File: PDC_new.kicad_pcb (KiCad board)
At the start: 2 copper layers, 97 parts, among them J1 Conn_01x02_Pin, J10 Conn_01x02_Pin, J12 Conn_01x02_Pin, J13 XT90PW-F, J14 B2B-XH-A__LF__SN_, J15 Conn_01x02, J2 Conn_01x02_Pin, J3 Conn_01x02_Pin, J4 Conn_01x02_Pin, J5 Conn_01x02_Pin, J6 Conn_01x02_Pin, J7 Conn_01x02_Pin, J8 Conn_01x02_Pin, J9 Conn_01x02_Pin, Q1 BSS123, Q2 IRF540NSTRLPBF, U1 TPSI3050QDWZRQ1, U10 LM393LVDR, U11 IPB017N10N5ATMA1, U12 IPB017N10N5ATMA1, U13 XT90PW(2+2)-M.G.Y, U14 IPB017N10N5ATMA1, U2 TPSI3050QDWZRQ1, U3 TPSI3050QDWZRQ1, U4 74HC74, U5 URB4805LD-60WR3, U6 IPB017N10N5ATMA1, U7 TLC555CDR, U8 SN74HC08D, U9 SN74HC14DR

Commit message: pcb: continue routing, add board outline, remove stray J15
Remove J15 footprint, which has no matching symbol in the schematic.
Mirror the same board into the top-level PDC_new.kicad_pcb.

Co-Authored-By: Claude Opus 5.5 <noreply@anthropic.com>
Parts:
- removed J15: Conn_01x02, Connector_JST:JST_XH_B2B-XH-A_1x02_P2.50mm_Vertical
- moved C6 196.5 mm to (341.1, 308.0)
- moved F1 189.6 mm to (243.0, 280.8)
- moved F3 184.7 mm to (281.5, 251.3)
- moved R4 178.8 mm to (308.9, 254.5)
- moved R6 176.4 mm to (304.0, 260.5)
- moved C18 170.2 mm to (345.0, 248.0)
- moved D5 162.2 mm to (314.0, 243.5), turned to 90 degrees
- moved C22 161.2 mm to (347.0, 231.5)
- moved R24 159.1 mm to (319.0, 236.4), turned to 90 degrees
- moved R22 158.0 mm to (308.9, 260.5)
- moved C25 154.9 mm to (330.0, 248.0)
- moved C19 146.8 mm to (319.0, 243.0), turned to 90 degrees
- moved R21 146.7 mm to (303.9, 255.0)
- moved C26 142.0 mm to (331.5, 232.0)
- moved C23 139.4 mm to (334.5, 216.0)
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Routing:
- net Net-(U3-VDDH): track 0.00 -> 3.13 mm

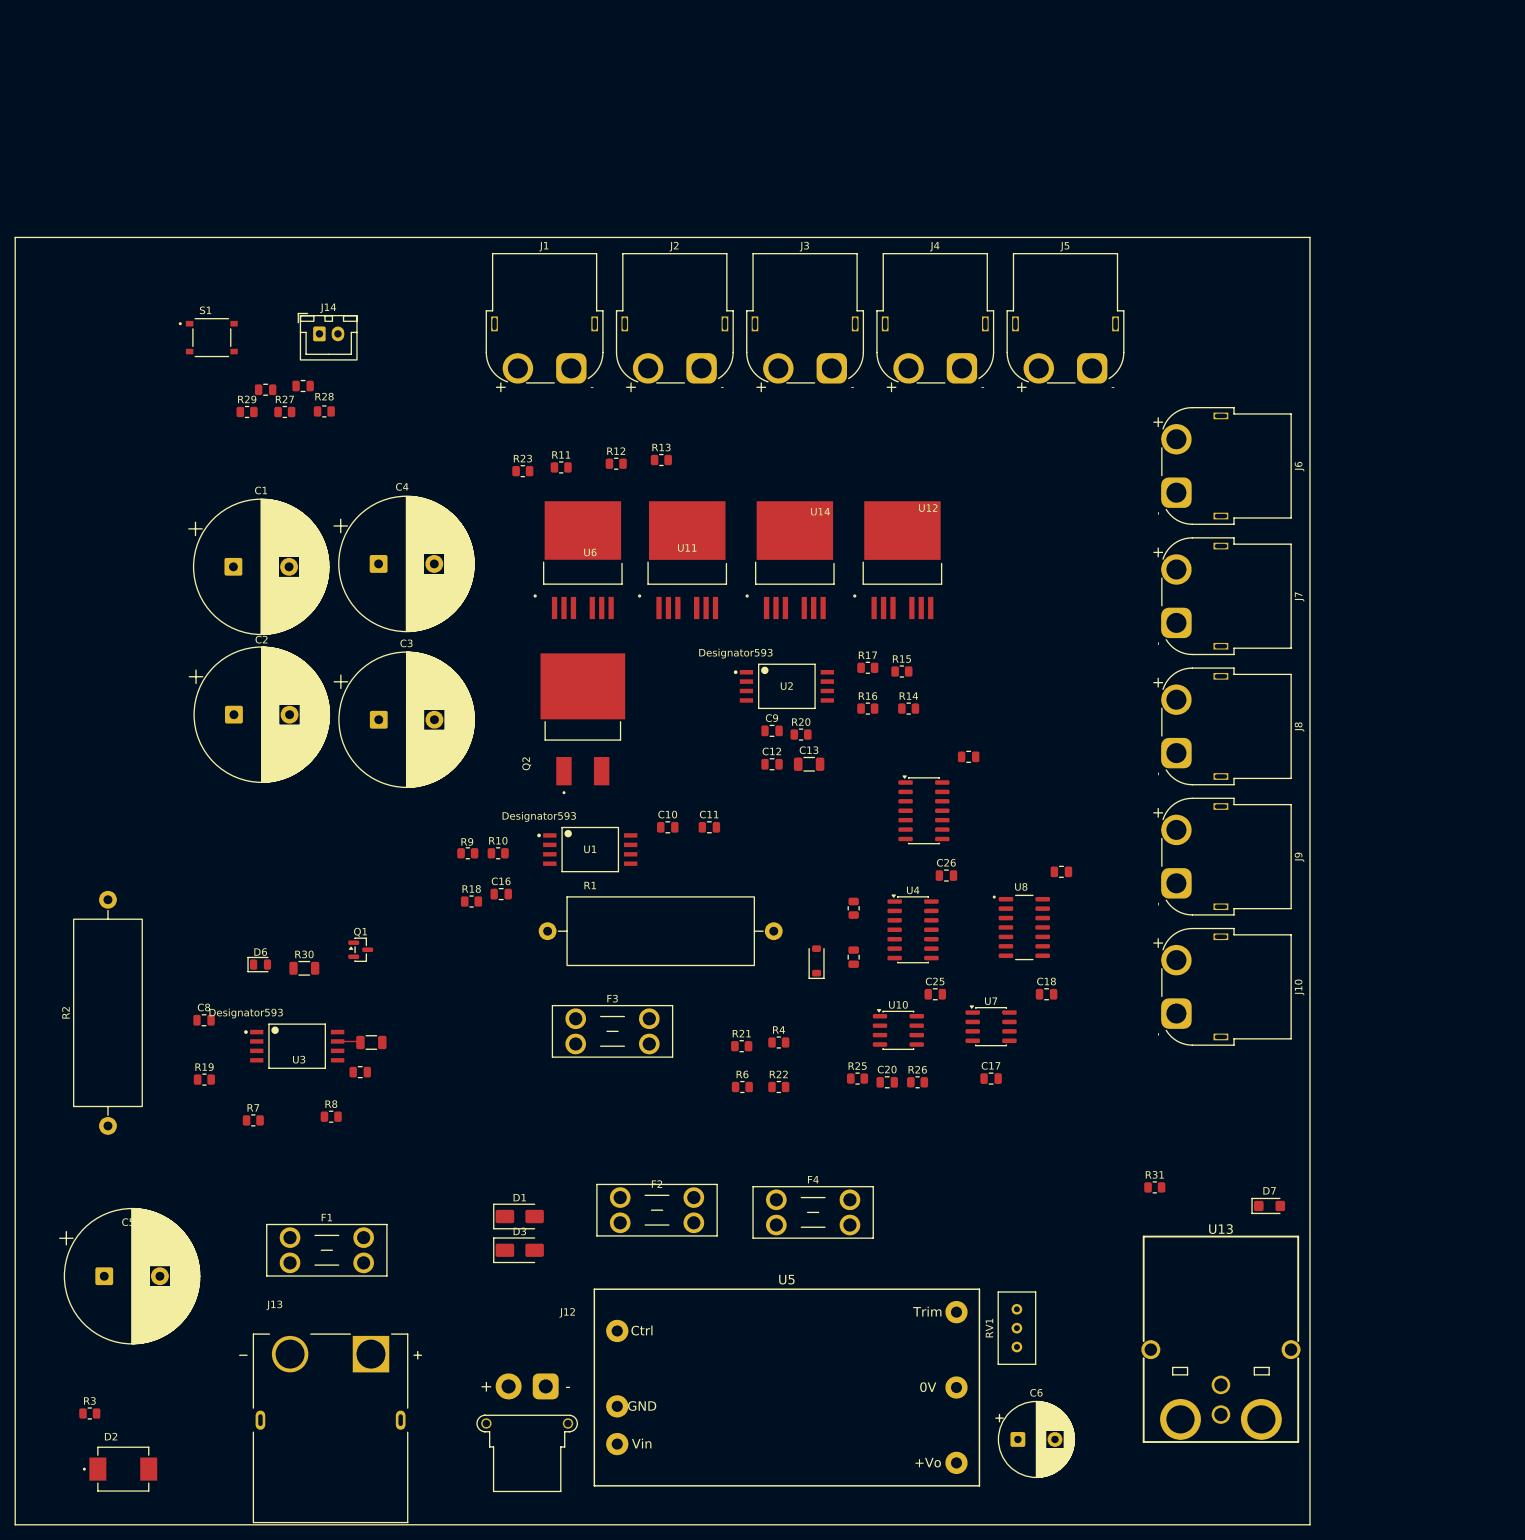
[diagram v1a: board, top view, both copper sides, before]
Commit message: Reorganize repo: move libraries into Libraries/, promote PDC_new (2) to main project
Libraries:
- Move all symbol/footprint folders into Libraries/: B2B-XH-A__LF__SN_,
  IRF540NSTRLPBF, SMCJ54A, SMCJ54CA-13-F, SN74HC08D, SN74HC14DR,
  TS-1187A-B-A-B, XT90PW-F, ul_LM393LVDR and pdc_new.pretty.
- Merge root ul_IPB017N10N5ATMA1/ and ul_TPSI3050QDWZRQ1/ into the existing
  folders in Libraries/ (KiCADv6 symbols/footprints moved in; duplicate
  readme.txt and ImportGuides.html at the root dropped).
- Update fp-lib-table and sym-lib-table to point at ${KIPRJMOD}/Libraries/.

Project files:
- Replace PDC_new.kicad_sch/.kicad_pcb/.kicad_pro with the latest
  PDC_new (2) versions and remove the PDC_new (2)/ folder.
- Move PDC_new (2)/report.txt to the repo root.
- Remove the stray extensionless "PDC_new" file (old schematic copy).
- Rename internal "PDC_new (2)" references (schematic instance project
  names, PCB sheetfile refs, project metadata) to "PDC_new".
- Change absolute C:/Users/... 3D model paths in the PCB to
  ${KIPRJMOD}/Libraries/... so they resolve on any machine.

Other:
- .history/ is already ignored by .gitignore (applies at any depth).
- Update README to describe the Libraries/ folder.

Co-Authored-By: Claude Opus 5.5 <noreply@anthropic.com>
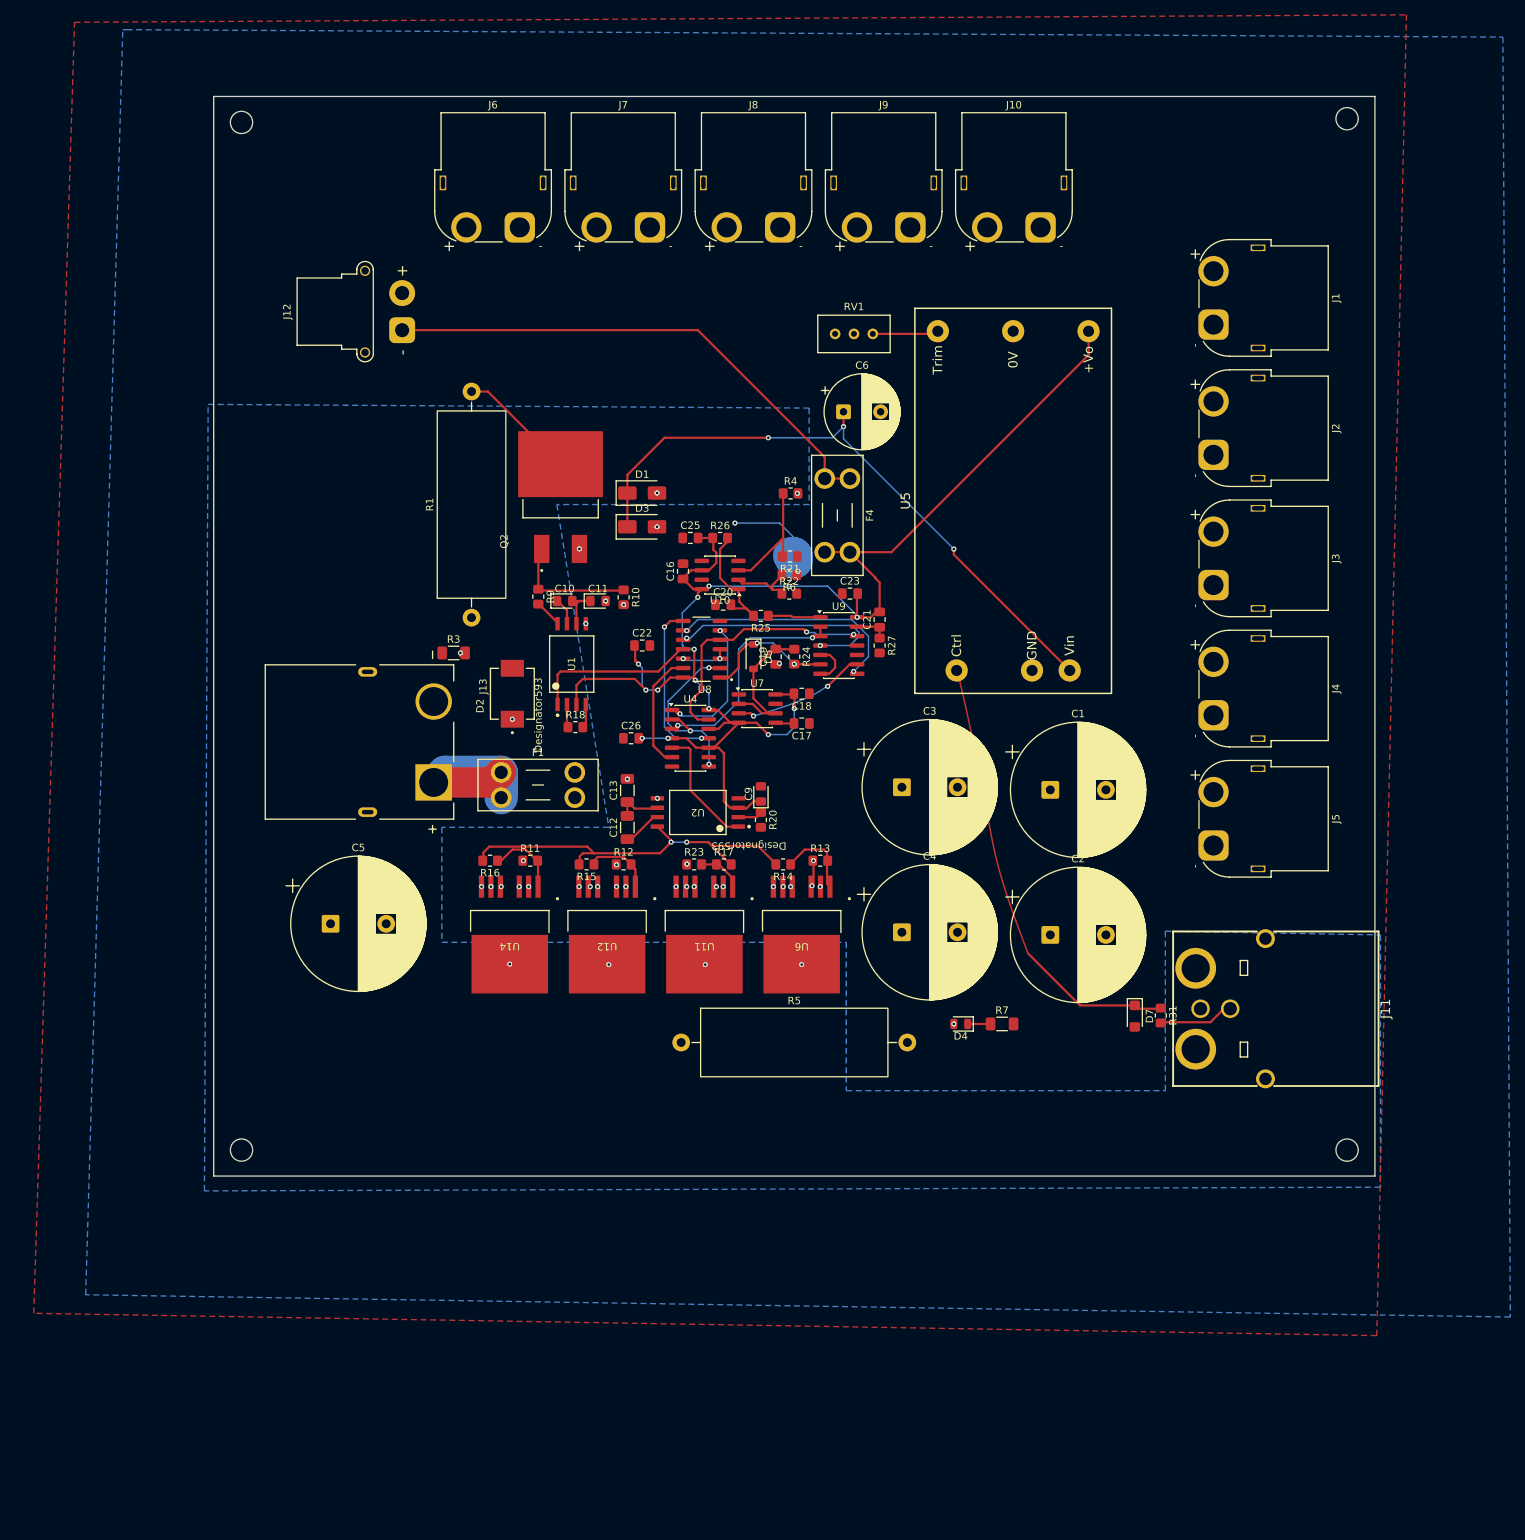
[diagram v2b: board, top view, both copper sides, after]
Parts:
- removed C14: 470nF, Capacitor_SMD:C_1206_3216Metric
- removed C15: 470nF, Capacitor_SMD:C_0805_2012Metric
- removed C24: 2.2µF, Capacitor_SMD:C_0805_2012Metric
- removed C8: 1µF, Capacitor_SMD:C_0805_2012Metric
- removed D6: LED, LED_SMD:LED_0805_2012Metric
- removed F2, F3: 3568-15, Fuse:Fuseholder_Blade_Mini_Keystone_3568
- removed J14: B2B-XH-A__LF__SN_, Connector_JST:JST_XH_B2B-XH-A_1x02_P2.50mm_Vertical
- removed Q1: BSS123, Package_TO_SOT_SMD:SOT-23
- removed R19: 20k, Resistor_SMD:R_0805_2012Metric
- removed R2: 1k, Resistor_THT:R_Axial_Power_L25.0mm_W9.0mm_P30.48mm
- removed R28, R29, R8: 10k, Resistor_SMD:R_0805_2012Metric
- removed R30: 22k, Resistor_SMD:R_1206_3216Metric
- removed S1: TS-1187A-B-A-B, TS-1187A-B-A-B:SW_TS-1187A-B-A-B
- removed U13: XT90PW(2+2)-M.G.Y, XT90I(2+2)PW-M:CONN-TH_XT90PW2X2-MGY
- removed U3: TPSI3050QDWZRQ1, ul_TPSI3050QDWZRQ1:DWZ0008A-MFG
- added D4: LED, LED_SMD:LED_0805_2012Metric, F.Cu at (333.4, 252.0)
- added J11: XT90PW(2+2)-M.G.Y, XT90PW(2+2)-M.G.Y:CONN-TH_XT90PW2X2-MGY, F.Cu at (369.8, 250.0)
- added R5: 1k, Resistor_THT:R_Axial_Power_L25.0mm_W9.0mm_P30.48mm, F.Cu at (295.8, 254.5)
- C10, C11, C9: footprint Capacitor_SMD:C_0805_2012Metric -> LED_SMD:LED_0805_2012Metric_Pad1.15x1.40mm_HandSolder
- C12: value 2.2µF -> 4.3µF; footprint Capacitor_SMD:C_0805_2012Metric -> Capacitor_SMD:C_1206_3216Metric_Pad1.33x1.80mm_HandSolder
- C13: value 2.2 µF -> 4.3 µF; footprint Capacitor_SMD:C_1206_3216Metric -> Capacitor_SMD:C_1206_3216Metric_Pad1.33x1.80mm_HandSolder
- C16, C17, C18, C19, C20, C21, C22, C23, C25, C26: footprint Capacitor_SMD:C_0805_2012Metric -> Capacitor_SMD:C_0805_2012Metric_Pad1.18x1.45mm_HandSolder
- C5, C6: value C -> 100uF
- R10, R11, R12, R13, R14, R15, R16, R17, R18, R20, R21, R22, R23, R24, R25, R26, R27, R31, R4, R6, R9: footprint Resistor_SMD:R_0805_2012Metric -> Resistor_SMD:R_0805_2012Metric_Pad1.20x1.40mm_HandSolder
- R3: footprint Resistor_SMD:R_0805_2012Metric -> Resistor_SMD:R_1206_3216Metric_Pad1.30x1.75mm_HandSolder
- R7: value 10 -> 22k; footprint Resistor_SMD:R_0805_2012Metric -> Resistor_SMD:R_1206_3216Metric_Pad1.30x1.75mm_HandSolder
- moved J12 143.7 mm to (258.1, 158.5), turned to 90 degrees
- moved C6 140.5 mm to (317.6, 169.5)
- moved RV1 132.9 mm to (321.6, 159.0), turned to 0 degrees
- moved U5 123.3 mm to (340.5, 181.5), turned to 90 degrees
- moved D2 116.9 mm to (273.0, 207.5), turned to 90 degrees
- moved C1 114.1 mm to (345.5, 220.4)
- moved C2 114.0 mm to (345.5, 240.0)
- moved R3 113.6 mm to (265.1, 202.0)
- moved J10 107.5 mm to (344.2, 144.7), turned to 0 degrees
- moved R7 101.7 mm to (339.0, 252.0)
- moved D1 98.9 mm to (290.5, 180.4)
- moved D3 98.9 mm to (290.5, 185.0)
- moved F4 97.7 mm to (318.5, 178.5), turned to -90 degrees
- moved J6 95.4 mm to (274.0, 144.7), turned to 0 degrees
- moved J9 95.4 mm to (326.6, 144.7), turned to 0 degrees
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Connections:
- net /POR_N renamed /reset_N
- net /POR_RC renamed /reset_rc
- net Net-(J13-POS) renamed /BATT_IN
- net Net-(Q2-Pad1) renamed /GATE_PRE
- net Net-(Q2-Pad2) renamed /PRE_DRAIN
- net Net-(U1-VDDH) renamed /U1_VDDH
- net Net-(U1-VDDM) renamed /U1_VDDM
- net Net-(U2-VDDH) renamed /U2_VDDH
- net Net-(U2-VDDM) renamed /U2_VDDM
- C6 pad 1: Net-(U5-Vin) -> /BUCK_IN
- D1 pad 1: Net-(D1-K) -> /BUCK_IN
- D3 pad 1: Net-(D1-K) -> /BUCK_IN
- R1 pad 1: Net-(F3-Pad2) -> /BATT+
- R7 pad 2: Net-(U3-VDRV) -> GND
- RV1 pad 2: Net-(U5-0V) -> GND
- RV1 pad 3: Net-(U5-0V) -> GND
- U5 pad 3: Net-(U5-Vin) -> /BUCK_IN
- U5 pad 5: Net-(U5-0V) -> GND
- U9 pad 10: /EN_BLEED -> unconnected-(U9-5Y-Pad10)
- U9 pad 11: /RUN_OK -> GND
- U9 pad 5: /MSTR_FILT -> GND
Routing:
- net /+5V: track 0.00 -> 204.8 mm, vias 0 -> 13
- net /BUCK_IN: track 0.00 -> 86.3 mm, vias 0 -> 3
- net Net-(J12-Pin_1): track 0.00 -> 70.3 mm
- net /GATE_MAIN: track 0.00 -> 53.4 mm, vias 0 -> 2
- net /reset_N: track 0.00 -> 35.1 mm, vias 0 -> 2
- net /TIMEOUT: track 0.00 -> 32.9 mm, vias 0 -> 2
- net /DONE_N: track 0.00 -> 31.2 mm, vias 0 -> 2
- net /PC_DONE: track 0.00 -> 30.5 mm, vias 0 -> 2
- net /FAULT_N: track 0.00 -> 25.1 mm, vias 0 -> 3
- net /FAULT_SET: track 0.00 -> 23.0 mm, vias 0 -> 2
- net /BATT_IN: track 0.00 -> 22.8 mm
- net /EN_PRE: track 0.00 -> 22.4 mm
- net /BUCK_CTRL: track 0.00 -> 21.0 mm
- net /TIMER_RC: track 0.00 -> 20.5 mm
- net /MSTR_ON: track 0.00 -> 19.3 mm, vias 0 -> 2
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- added copper zone on B.Cu, net /BATT+
- added copper zone on B.Cu, net /BUS+
- added copper zone on F.Cu, net GND
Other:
- board outline added: 156.5 x 145.5 mm
